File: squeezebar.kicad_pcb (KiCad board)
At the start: 2 copper layers, 106 x 20.3 mm, 43 parts, among them J1 RESET, J2 Conn_02x08_Counter_Clockwise, J3 I2C, U1 Elite-C

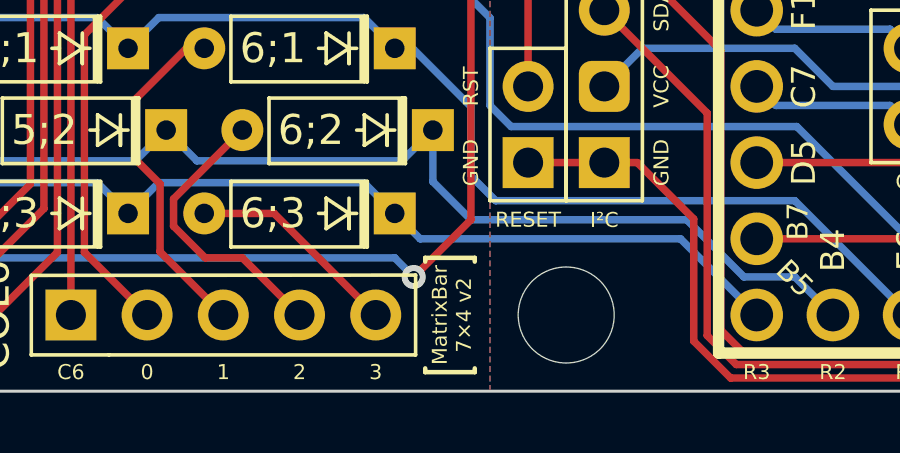
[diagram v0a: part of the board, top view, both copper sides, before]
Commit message: Rename to Squeezebar again
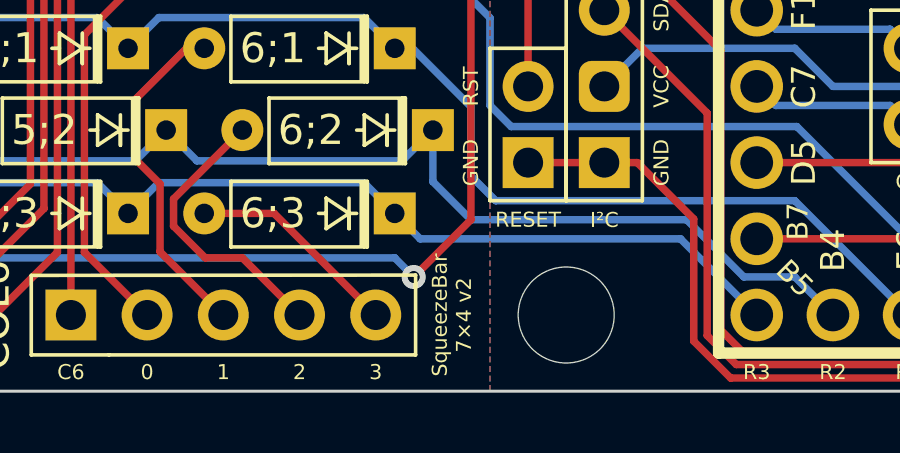
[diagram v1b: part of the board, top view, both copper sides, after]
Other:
- board text added: "SqueezeBar 7×4 v2"
- board text removed: "MatrixBar 7×4 v2"
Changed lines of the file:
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@@
     )
   )
-  (gr_line (start 93.091 74.422) (end 93.091 74.295001) (layer "B.SilkS") (width 0.15))
-  (gr_line (start 94.741999 78.104999) (end 94.741999 77.978) (layer "B.SilkS") (width 0.15))
-  (gr_line (start 93.091 77.978) (end 93.091 78.105) (layer "B.SilkS") (width 0.15))
-  (gr_line (start 94.742 74.295) (end 94.741999 74.422001) (layer "B.SilkS") (width 0.15))
-  (gr_line (start 93.091 78.105) (end 94.741999 78.104999) (layer "B.SilkS") (width 0.15))
   (gr_line (start 101.6 58.42) (end 101.6 78.74) (layer "B.SilkS") (width 0.15))
-  (gr_line (start 93.091 74.295001) (end 94.742 74.295) (layer "B.SilkS") (width 0.15))
-  (gr_line (start 94.741999 74.295001) (end 93.091 74.295001) (layer "F.SilkS") (width 0.15))
-  (gr_line (start 93.091 74.295001) (end 93.091 74.422) (layer "F.SilkS") (width 0.15))
-  (gr_line (start 94.741999 74.422) (end 94.741999 74.295001) (layer "F.SilkS") (width 0.15))
-  (gr_line (start 93.091 78.104999) (end 93.091 77.978) (layer "F.SilkS") (width 0.15))
   (gr_line (start 28.989248 28.444184) (end 43.357658 14.075774) (layer "F.SilkS") (width 0.15))
-  (gr_line (start 94.741999 77.977999) (end 94.742 78.105) (layer "F.SilkS") (width 0.15))
-  (gr_line (start 94.742 78.105) (end 93.091 78.104999) (layer "F.SilkS") (width 0.15))
   (gr_line (start 133.985 77.47) (end 133.985 59.69) (layer "Edge.Cuts") (width 0.1))
   (gr_line (start 30.48 78.74) (end 132.715 78.74) (layer "Edge.Cuts") (width 0.1))
@@
     (effects (font (size 0.5 0.5) (thickness 0.125)) (justify mirror))
   )
-  (gr_text "MatrixBar\n7×4 v2\n" (at 93.98 76.2 90) (layer "B.SilkS")
+  (gr_text "SqueezeBar\n7×4 v2\n" (at 93.98 76.2 90) (layer "B.SilkS")
     (effects (font (size 0.5 0.5) (thickness 0.1)) (justify mirror))
   )
@@
     (effects (font (size 0.5 0.5) (thickness 0.125)))
   )
-  (gr_text "MatrixBar\n7×4 v2\n" (at 93.98 76.2 90) (layer "F.SilkS")
+  (gr_text "SqueezeBar\n7×4 v2\n" (at 93.98 76.2 90) (layer "F.SilkS")
     (effects (font (size 0.5 0.5) (thickness 0.1)))
   )

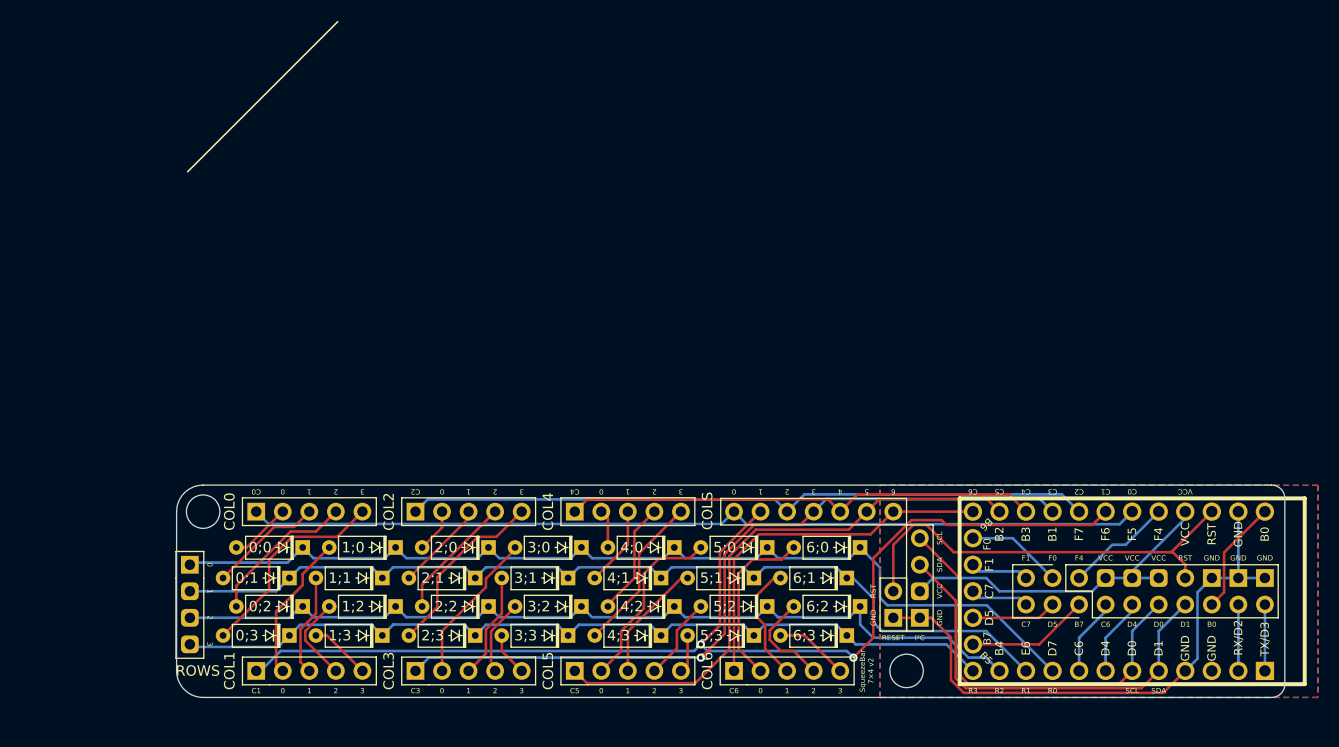
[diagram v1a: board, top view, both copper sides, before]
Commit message: Squeezebar: Make it passive, with JST connectors
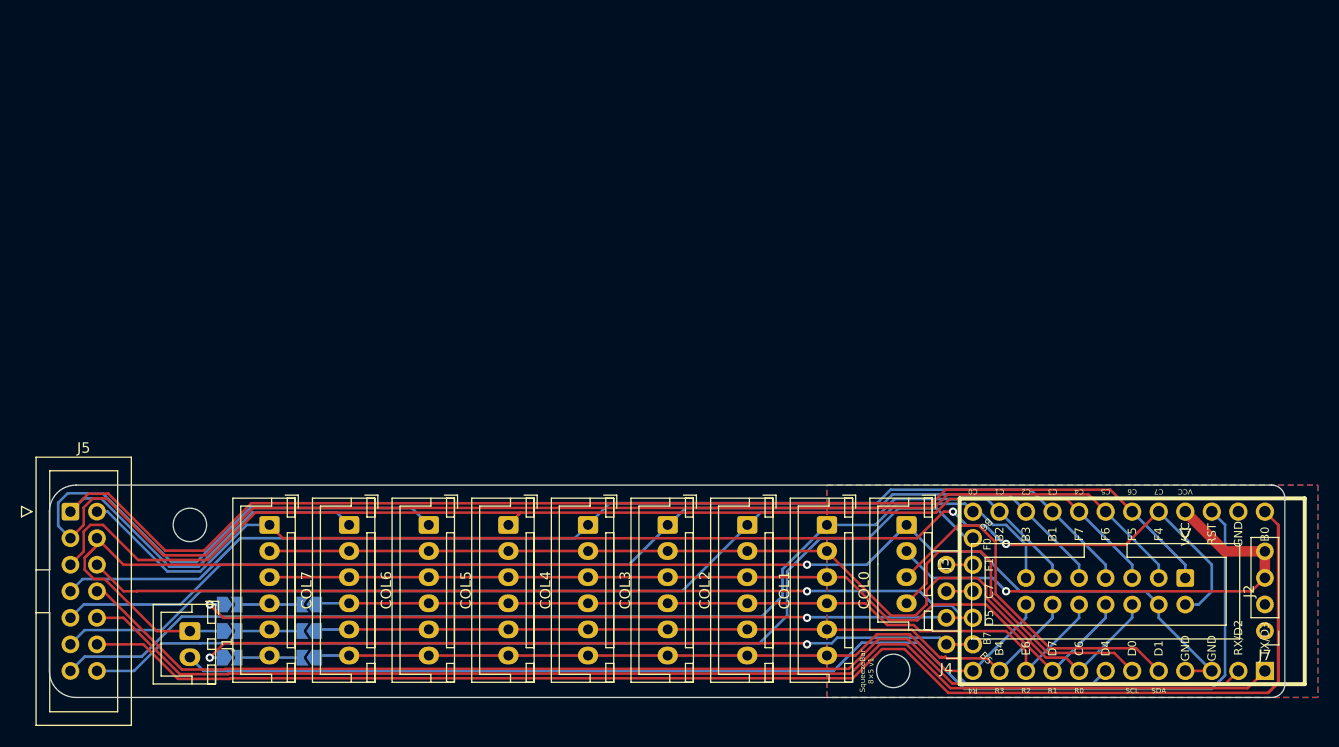
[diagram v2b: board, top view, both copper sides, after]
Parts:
- removed 0;0, 0;1, 0;2, 0;3, 1;0, 1;1, 1;2, 1;3, 2;0, 2;1, 2;2, 2;3, 3;0, 3;1, 3;2, 3;3, 4;0, 4;1, 4;2, 4;3, 5;0, 5;1, 5;2, 5;3, 6;0, 6;1, 6;2, 6;3: D, Library:Diode
- removed COLUMNS1: PINSOCKET, Library:PinHeader_COLS_1x07_P2.54mm_Vertical
- removed ROWS2: PINSOCKET, Library:PinSocket_1x04_P2.54mm_Vertical_LongPads
- added COL7: COL7, Connector_JST:JST_XH_B6B-XH-A_1x06_P2.50mm_Vertical, F.Cu at (36.8, 62.2)
- added J4: XTRA, Connector_PinHeader_2.54mm:PinHeader_1x04_P2.54mm_Vertical, F.Cu at (101.6, 73.7)
- added J5: Conn_02x08_Counter_Clockwise, Connector_IDC:IDC-Header_2x07_P2.54mm_Vertical, F.Cu at (17.8, 61.0)
- added J7: PWR, Connector_PinHeader_2.54mm:PinHeader_1x04_P2.54mm_Vertical, F.Cu at (132.1, 72.4)
- added JP1: Jumper_2_Open, Jumper:SolderJumper-2_P1.3mm_Open_TrianglePad1.0x1.5mm, B.Cu at (40.6, 74.9)
- added JP2: Jumper_2_Open, Jumper:SolderJumper-2_P1.3mm_Open_TrianglePad1.0x1.5mm, B.Cu at (33.0, 74.9)
- added JP3: Jumper_2_Open, Jumper:SolderJumper-2_P1.3mm_Open_TrianglePad1.0x1.5mm, B.Cu at (40.6, 72.4)
- added JP4: Jumper_2_Open, Jumper:SolderJumper-2_P1.3mm_Open_TrianglePad1.0x1.5mm, B.Cu at (33.0, 72.4)
- added JP5: Jumper_2_Open, Jumper:SolderJumper-2_P1.3mm_Open_TrianglePad1.0x1.5mm, B.Cu at (40.6, 69.8)
- added JP6: Jumper_2_Open, Jumper:SolderJumper-2_P1.3mm_Open_TrianglePad1.0x1.5mm, B.Cu at (33.0, 69.8)
- COL0, COL1, COL2, COL3, COL4, COL5, COL6: footprint Library:PinHeader_Col_1x05_P2.54mm_Vertical -> Connector_JST:JST_XH_B6B-XH-A_1x06_P2.50mm_Vertical
- J1: footprint Library:PinHeader_RST_1x02_P2.54mm_Vertical -> Connector_JST:JST_XH_B2B-XH-A_1x02_P2.50mm_Vertical
- J2: footprint Library:PinSocket_2x10_P2.54mm_Bespoke -> Connector_IDC:IDC-Header_2x07_P2.54mm_Vertical
- J3: footprint Library:PinHeader_I2C_1x04_P2.54mm_Vertical -> Connector_JST:JST_XH_B4B-XH-A_1x04_P2.50mm_Vertical; moved to F.Cu
- moved J1 67.3 mm to (29.2, 72.4), turned to -90 degrees
- moved COL0 54.6 mm to (90.2, 62.2), turned to -90 degrees
- moved COL1 49.0 mm to (82.5, 62.2), turned to -90 degrees
- moved COL6 39.4 mm to (44.5, 62.2), turned to -90 degrees
- moved COL2 24.2 mm to (74.9, 62.2), turned to -90 degrees
- moved COL3 21.6 mm to (67.3, 62.2), turned to -90 degrees
- moved COL5 19.8 mm to (52.1, 62.2), turned to -90 degrees
- moved J3 8.98 mm to (97.8, 62.2), turned to -90 degrees
- moved J2 8.03 mm to (124.5, 67.3)
- moved COL4 6.48 mm to (59.7, 62.2), turned to -90 degrees
- moved H4 1.80 mm to (29.2, 62.2)
- moved H2 1.27 mm to (96.5, 76.2)
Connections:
- COL0 pad 2: Net-(0;0-Pad2) -> /r0
- COL0 pad 3: Net-(0;1-Pad2) -> /r1
- COL0 pad 4: Net-(0;2-Pad2) -> /r2
- COL0 pad 5: Net-(0;3-Pad2) -> /r3
- COL1 pad 2: Net-(1;0-Pad2) -> /r0
- COL1 pad 3: Net-(1;1-Pad2) -> /r1
- COL1 pad 4: Net-(1;2-Pad2) -> /r2
- COL1 pad 5: Net-(1;3-Pad2) -> /r3
- COL2 pad 2: Net-(2;0-Pad2) -> /r0
- COL2 pad 3: Net-(2;1-Pad2) -> /r1
- COL2 pad 4: Net-(2;2-Pad2) -> /r2
- COL2 pad 5: Net-(2;3-Pad2) -> /r3
- COL3 pad 2: Net-(3;0-Pad2) -> /r0
- COL3 pad 3: Net-(3;1-Pad2) -> /r1
- COL3 pad 4: Net-(3;2-Pad2) -> /r2
- COL3 pad 5: Net-(3;3-Pad2) -> /r3
- COL4 pad 2: Net-(4;0-Pad2) -> /r0
- COL4 pad 3: Net-(4;1-Pad2) -> /r1
- COL4 pad 4: Net-(4;2-Pad2) -> /r2
- COL4 pad 5: Net-(4;3-Pad2) -> /r3
- COL5 pad 2: Net-(5;0-Pad2) -> /r0
- COL5 pad 3: Net-(5;1-Pad2) -> /r1
- COL5 pad 4: Net-(5;2-Pad2) -> /r2
- COL5 pad 5: Net-(5;3-Pad2) -> /r3
- COL6 pad 2: Net-(6;0-Pad2) -> /r0
- COL6 pad 3: Net-(6;1-Pad2) -> /r1
- COL6 pad 4: Net-(6;2-Pad2) -> /r2
- COL6 pad 5: Net-(6;3-Pad2) -> /r3
- J2 pad 1: /pd3 -> /c6
- J2 pad 10: /vcc -> /r2
- J2 pad 11: /pd4 -> /c1
- J2 pad 12: /vcc -> /r3
- J2 pad 13: /pc6 -> /c0
- J2 pad 14: /vcc -> /r4
- J2 pad 2: /gnd -> /c7
- J2 pad 3: /pd2 -> /c5
- J2 pad 5: /pb0 -> /c4
- J2 pad 6: /gnd -> /r0
- J2 pad 7: /sda -> /c3
- J2 pad 8: /rst -> /r1
- J2 pad 9: /scl -> /c2
- U1 pad 1: /pd3 -> /s2
- U1 pad 10: /r1 -> /r2
- U1 pad 11: /r2 -> /r3
- U1 pad 12: /r3 -> /r4
- U1 pad 13: /c6 -> /c0
- U1 pad 14: /c5 -> /c1
- U1 pad 15: /c4 -> /c2
- U1 pad 17: /c2 -> /c4
- U1 pad 18: /c1 -> /c5
- U1 pad 19: /c0 -> /c6
- U1 pad 2: /pd2 -> /s1
- U1 pad 20: /pf4 -> /c7
- U1 pad 24: /pb0 -> /s3
- U1 pad 25: /pb7 -> /t0
- U1 pad 26: /pd5 -> /t1
- U1 pad 27: /pc7 -> /t2
- U1 pad 28: /pf1 -> /t3
- U1 pad 29: /pf0 -> /s4
- U1 pad 7: /pd4 -> /s0
- U1 pad 8: /pc6 -> /r0
- U1 pad 9: /r0 -> /r1
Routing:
- net /s3: track 0.00 -> 151.1 mm
- net /c7: track 0.00 -> 123.7 mm, vias 0 -> 2
- net /s2: track 0.00 -> 117.6 mm
- net /s1: track 0.00 -> 115.1 mm
- net /c6: track 35.4 -> 148.8 mm
- net /c5: track 54.1 -> 160.7 mm
- net /s0: track 0.00 -> 105.4 mm, vias 0 -> 1
- net /s4: track 0.00 -> 93.3 mm
- net /gnd: track 55.5 -> 138.3 mm, vias 0 -> 1
- net /rst: track 41.5 -> 119.3 mm
- net /t0: track 0.00 -> 75.1 mm, vias 0 -> 2
- net /t1: track 0.00 -> 74.7 mm, vias 0 -> 2
- net /r4: track 0.00 -> 73.3 mm
- net /c4: track 45.5 -> 113.6 mm
- net /c2: track 65.8 -> 105.5 mm
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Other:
- board size 106 x 20.3 mm -> 118.2 x 20.3 mm
- board text added: "R4"
- board text added: "SqueezeBar 8×5 v1"
- board text removed: "0"
- board text removed: "1"
- board text removed: "2"
- board text removed: "3"
- board text removed: "4"
- board text removed: "5"
- board text removed: "6"
- board text removed: "B0"
- board text removed: "B7"
- board text removed: "COL0"
- board text removed: "COL1"
- board text removed: "COL2"
- board text removed: "COL3"
- board text removed: "COL4"
- board text removed: "COL5"
- board text removed: "COL6"
- board text removed: "COLS"
- board text removed: "D0"
- board text removed: "D1"
- board text removed: "D4"
- board text removed: "D5"
- board text removed: "F0"
- board text removed: "F1"
- board text removed: "F4"
- board text removed: "GND"
- board text removed: "I²C"
- board text removed: "RESET"
- board text removed: "ROWS"
- board text removed: "RST"
- board text removed: "SqueezeBar 7×4 v2"
